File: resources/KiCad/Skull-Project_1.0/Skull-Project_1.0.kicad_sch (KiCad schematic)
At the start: 8 parts, among them SW1 SW_SPST, SW2 SW_SPST

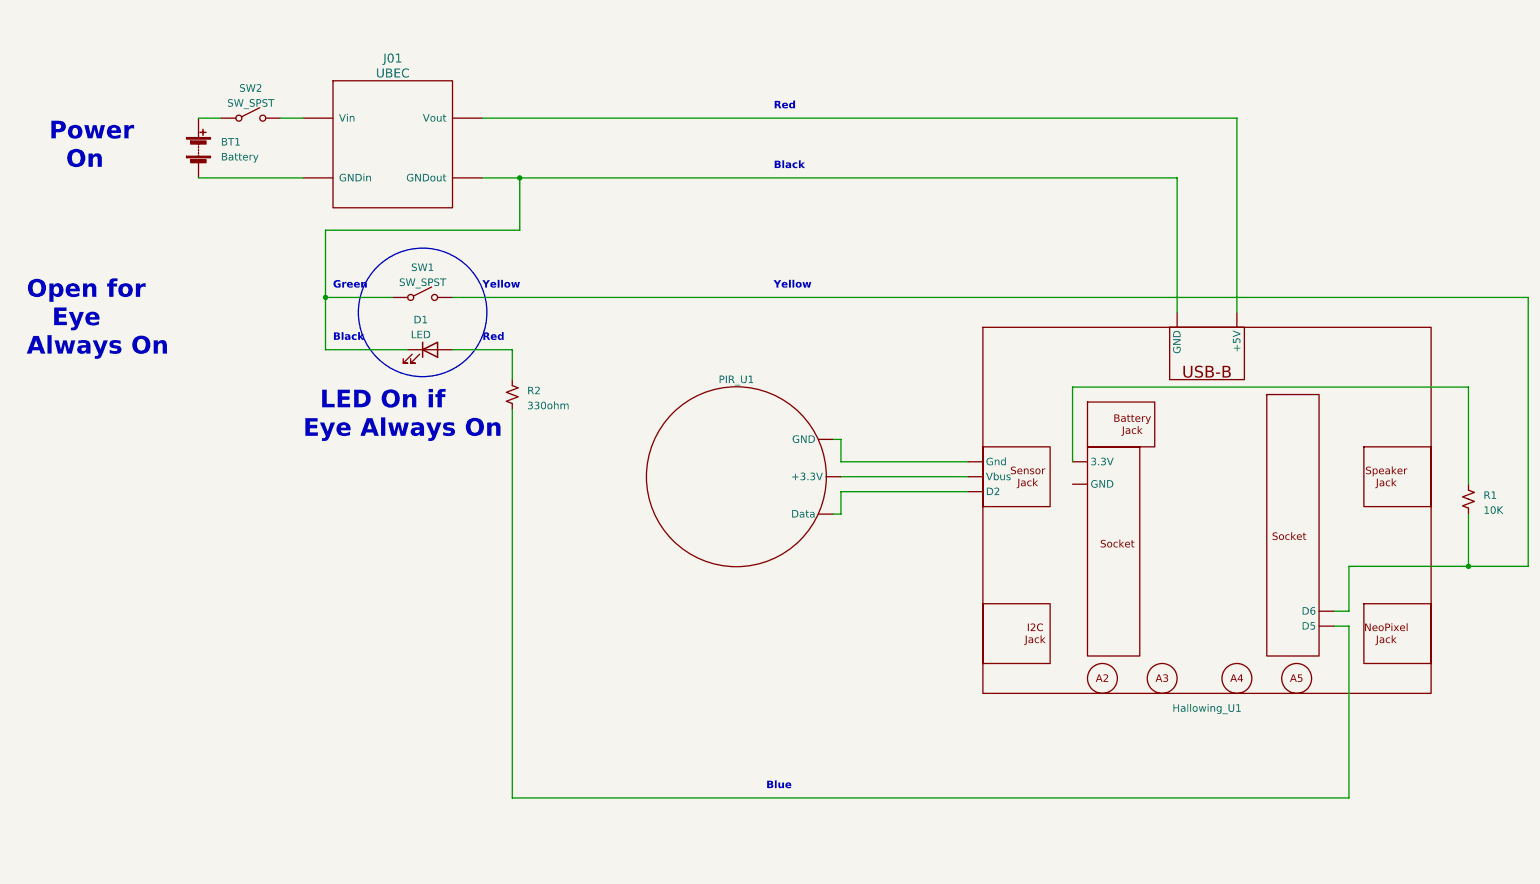
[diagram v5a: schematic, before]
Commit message: schematic update
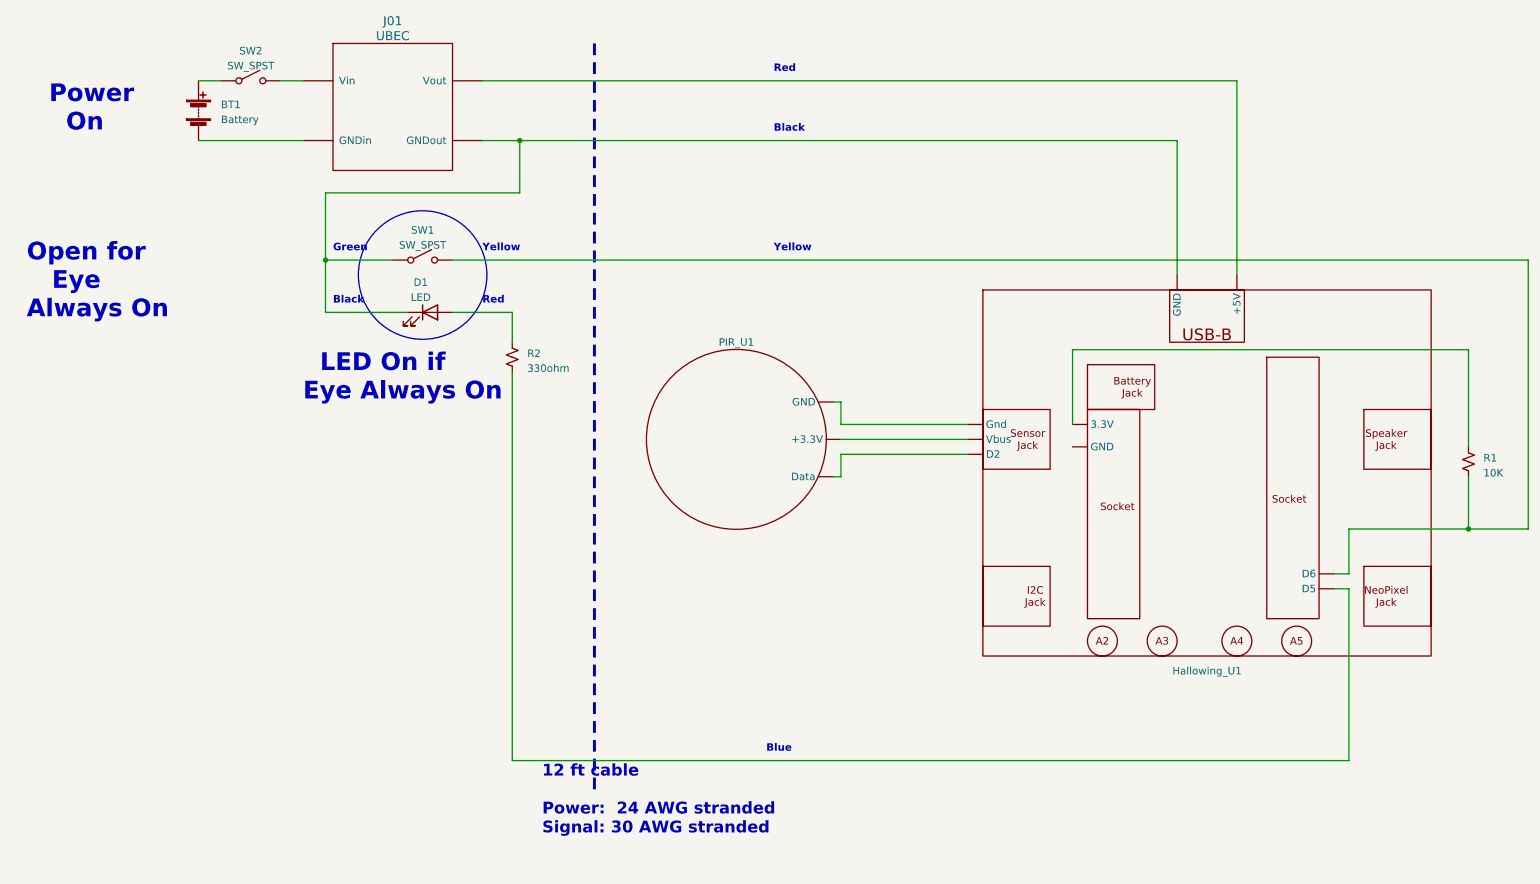
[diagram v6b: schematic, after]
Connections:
- net at Hallowing_U1. (Vbus): now also PIR_U1. (GND)
- net at SW2.~ (B): now also BT1.1 (+)
- new net: Hallowing_U1. (Vbus), R1.2, SW1.~ (B)
- new net: Hallowing_U1. (Vbus), PIR_U1. (GND) (x2)
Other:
- note added: "12 ft cable Power: 24 AWG stranded Signal: 30 AWG stranded"
- moved on the sheet: BT1, D1, Hallowing_U1, PIR_U1, R1, R2, SW1, SW2

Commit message: schematic update
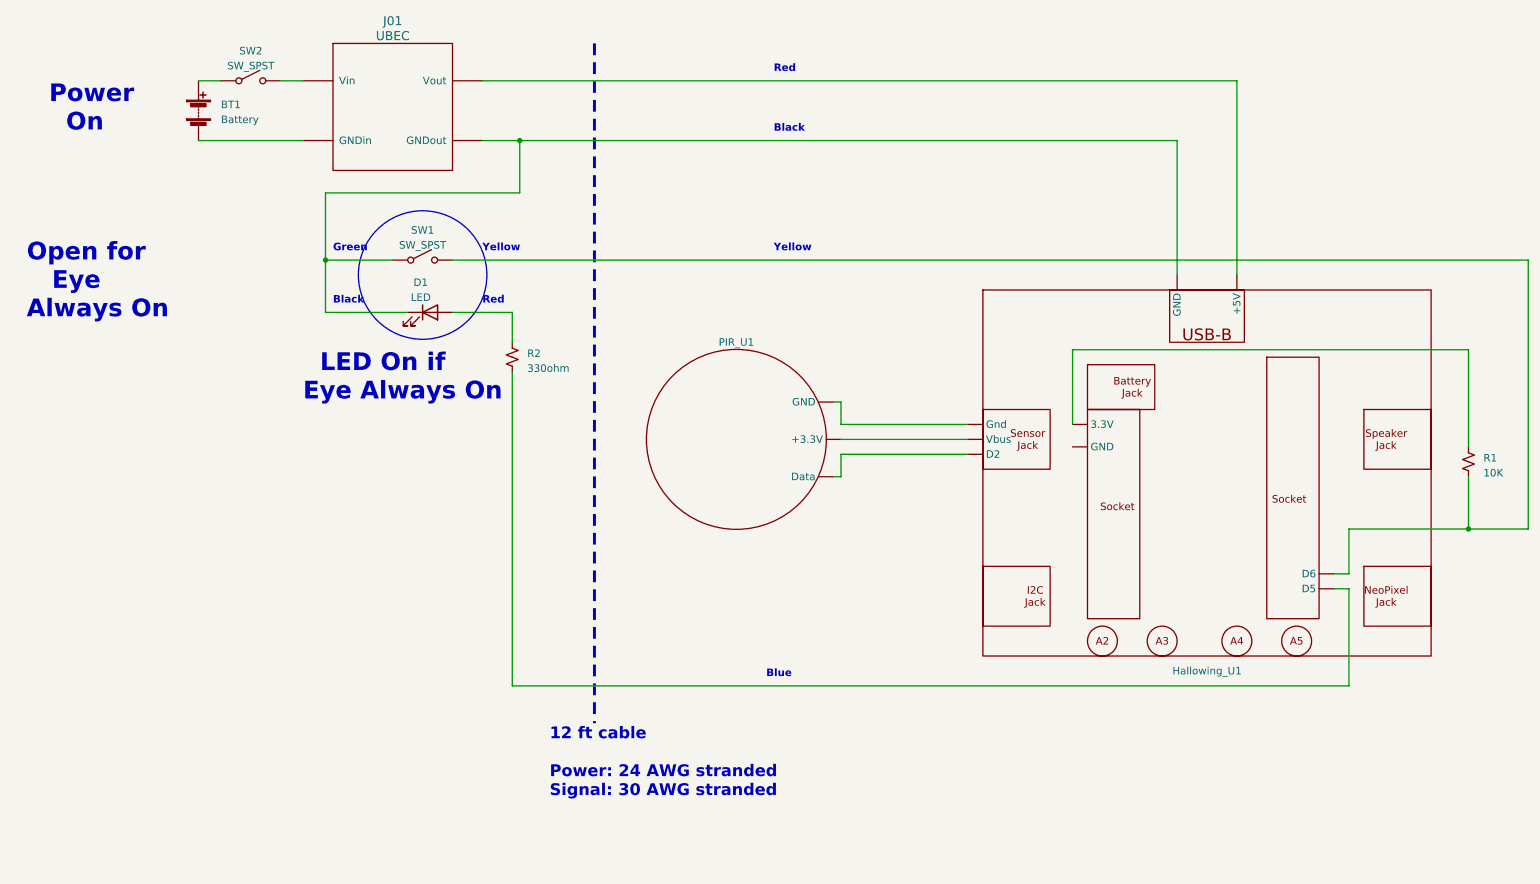
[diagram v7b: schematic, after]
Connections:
- net at Hallowing_U1. (Vbus): now also PIR_U1. (GND)
- net at SW2.~ (B): now also BT1.1 (+)
- new net: Hallowing_U1. (Vbus), R1.2, SW1.~ (B)
- new net: Hallowing_U1. (Vbus), PIR_U1. (GND) (x2)
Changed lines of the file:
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@@
   (title_block
     (title "Skull-Project 1.0")
-    (date "2024-09-03")
+    (date "2024-09-04")
     (rev "1.0")
     (company "github.com/Mark-MDO47/Skull-Project")
@@
     (stroke (width 0) (type default))
   )
-  (wire (pts (xy 245.11 114.3) (xy 245.11 143.51))
+  (wire (pts (xy 245.11 114.3) (xy 245.11 130.81))
     (stroke (width 0) (type default))
   )
@@
     (stroke (width 0) (type default))
   )
-  (polyline (pts (xy 116.84 21.59) (xy 116.84 148.59))
+  (polyline (pts (xy 116.84 21.59) (xy 116.84 137.16))
     (stroke (width 0.5) (type dash))
   )
@@
     (stroke (width 0) (type default))
   )
-  (wire (pts (xy 102.87 77.47) (xy 102.87 143.51))
+  (wire (pts (xy 102.87 77.47) (xy 102.87 130.81))
     (stroke (width 0) (type default))
   )
@@
     (stroke (width 0) (type default))
   )
-  (wire (pts (xy 245.11 143.51) (xy 102.87 143.51))
+  (wire (pts (xy 245.11 130.81) (xy 102.87 130.81))
     (stroke (width 0) (type default))
   )
@@
     (effects (font (size 1.27 1.27) bold) (justify left bottom))
   )
-  (text "Blue" (at 146.05 142.24 0)
+  (text "Blue" (at 146.05 129.54 0)
     (effects (font (size 1.27 1.27) bold) (justify left bottom))
   )
@@
     (effects (font (size 1.27 1.27) bold) (justify left bottom))
   )
-  (text "12 ft cable\n\nPower:  24 AWG stranded\nSignal: 30 AWG stranded"
-    (at 107.95 156.21 0)
+  (text "12 ft cable\n\nPower: 24 AWG stranded\nSignal: 30 AWG stranded"
+    (at 109.22 149.86 0)
     (effects (font (size 2 2) (thickness 0.4) bold) (justify left bottom))
   )

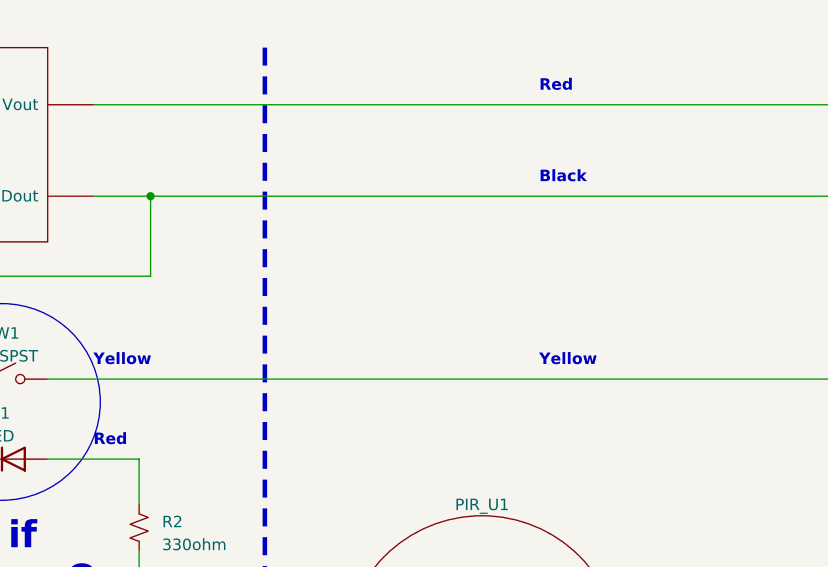
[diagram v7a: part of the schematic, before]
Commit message: schematic add warning to pull cable through before soldering
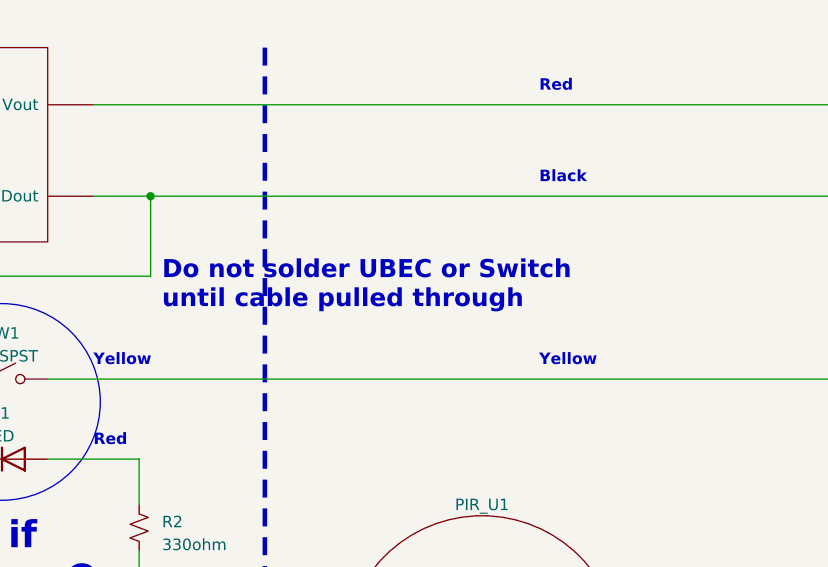
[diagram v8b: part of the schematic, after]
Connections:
- net at Hallowing_U1. (Vbus): now also PIR_U1. (GND)
- net at SW2.~ (B): now also BT1.1 (+)
- new net: Hallowing_U1. (Vbus), R1.2, SW1.~ (B)
- new net: Hallowing_U1. (Vbus), PIR_U1. (GND) (x2)
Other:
- note added: "Do not solder UBEC or Switch until cable pulled through"
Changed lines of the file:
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@@
   (title_block
     (title "Skull-Project 1.0")
-    (date "2024-09-04")
+    (date "2024-09-05")
     (rev "1.0")
     (company "github.com/Mark-MDO47/Skull-Project")
@@
     (effects (font (size 2 2) (thickness 0.4) bold) (justify left bottom))
   )
+  (text "Do not solder UBEC or Switch\nuntil cable pulled through"
+    (at 105.41 50.8 0)
+    (effects (font (size 2 2) (thickness 0.4) bold) (justify left bottom))
+  )
